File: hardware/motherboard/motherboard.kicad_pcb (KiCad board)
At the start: 4 copper layers, 152 x 68 mm, 81 parts, among them J1 IMU Connector, J2 JST-VH, J3 JST-VH, J4 JST-PH, J5 USB C 2.0, Q1 TSM7P06CP_ROG, Q2 TSM7P06CP_ROG, SW1 A, SW10 Right, SW11 Left, SW12 Up, SW2 B, SW3 X, SW4 Y, SW5 LB, SW6 RB, SW7 Start, SW8 Select, SW9 Down, U1 ESP32-S3-WROOM-1, U2 MCP73831-2-OT, U3 TPS75533KTTRG3, U4 TLV75709PDBV, U5 COM-09032

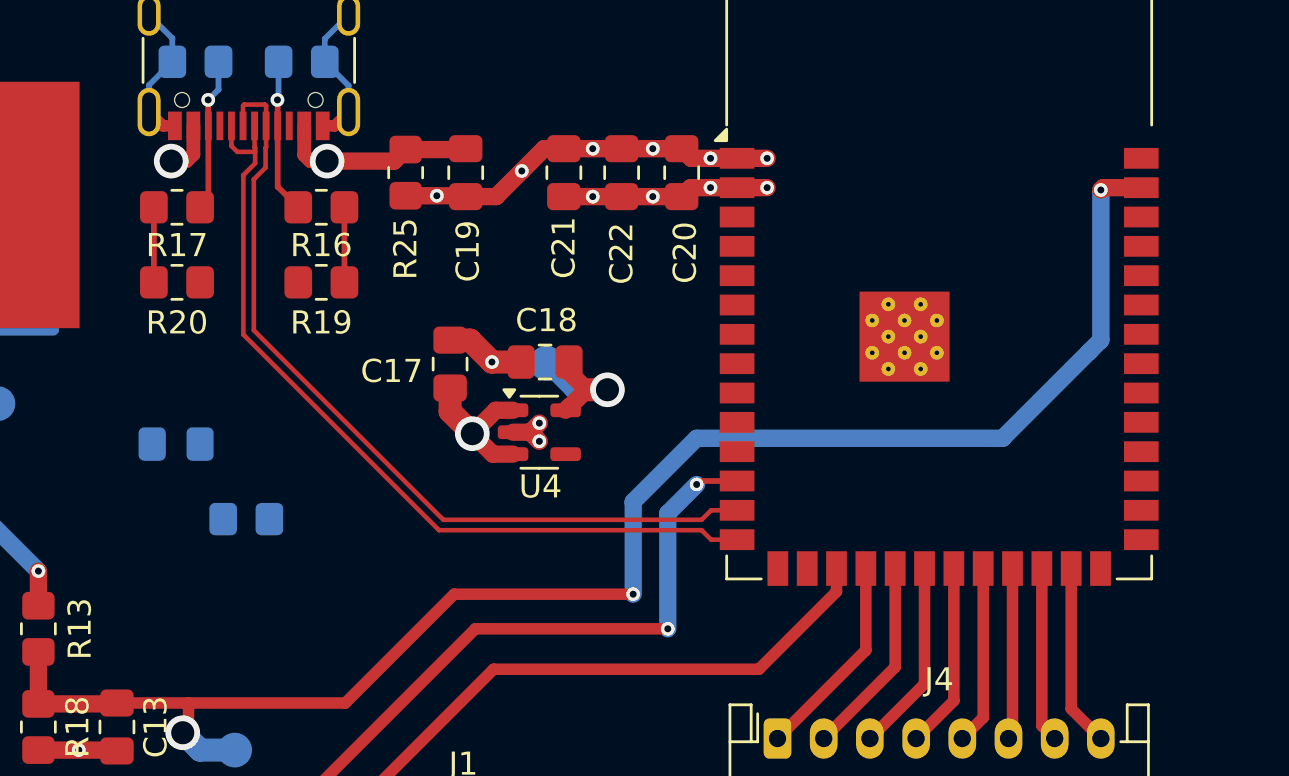
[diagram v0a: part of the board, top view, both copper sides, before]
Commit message: Reset Button
SMD Reset button on back behind MCU
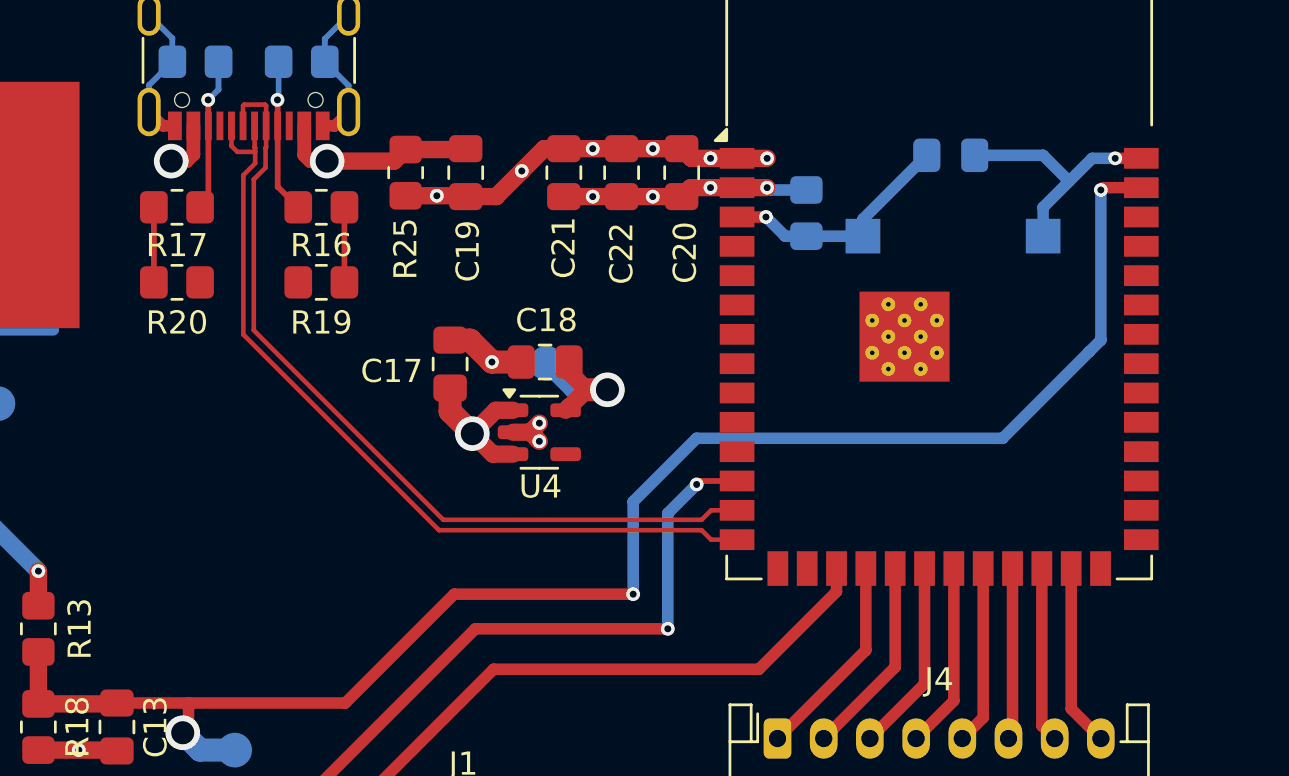
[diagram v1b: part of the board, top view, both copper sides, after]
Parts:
- added SW13: Reset, Button_Switch_SMD:SW_SPST_CK_RS282G05A3, B.Cu at (118.6, 23.2)
- moved C14 35.8 mm to (118.5, 19.8), turned to 0 degrees
- moved R14 27.6 mm to (112.2, 22.2), turned to 90 degrees
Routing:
- net GND: track 224.8 -> 235.7 mm, vias 15 -> 16
- net En: track 2.81 -> 13.5 mm, vias 0 -> 1
- net +3V3: track 34.8 -> 36.5 mm

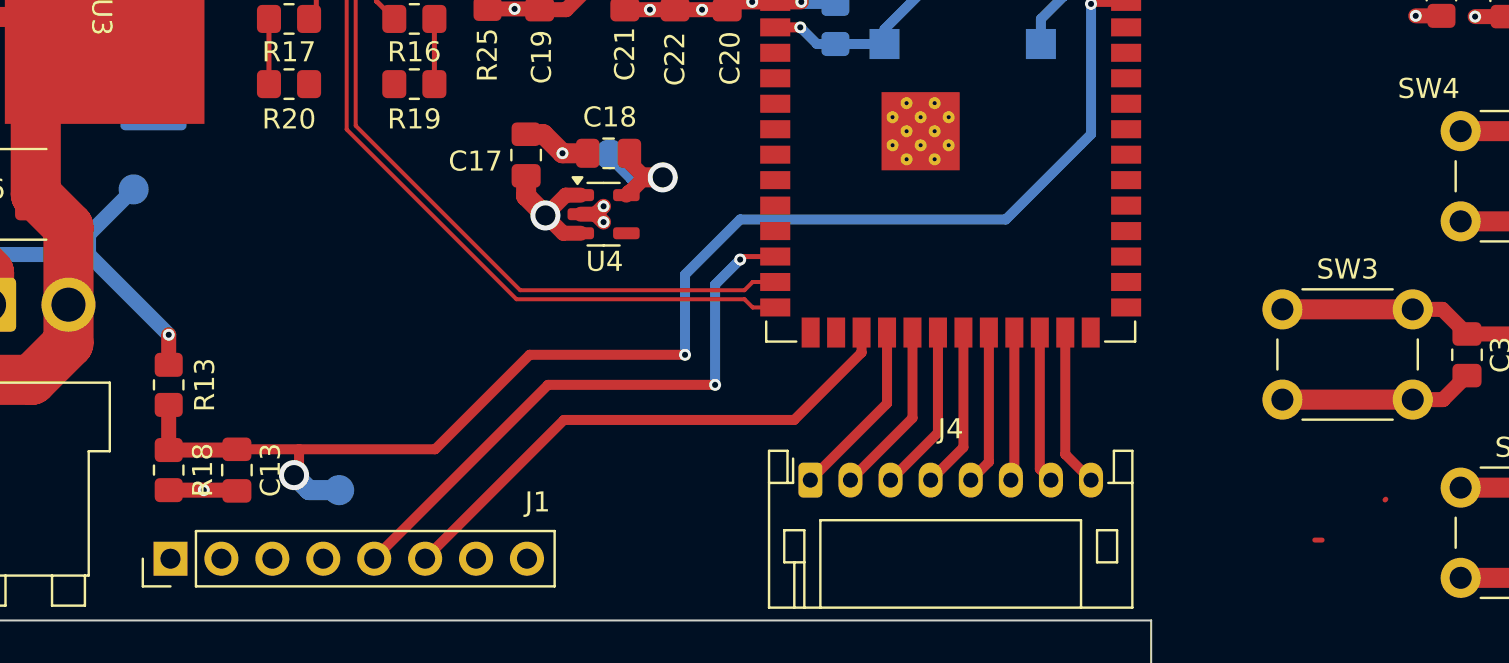
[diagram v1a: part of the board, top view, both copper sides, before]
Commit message: Added IMU Model
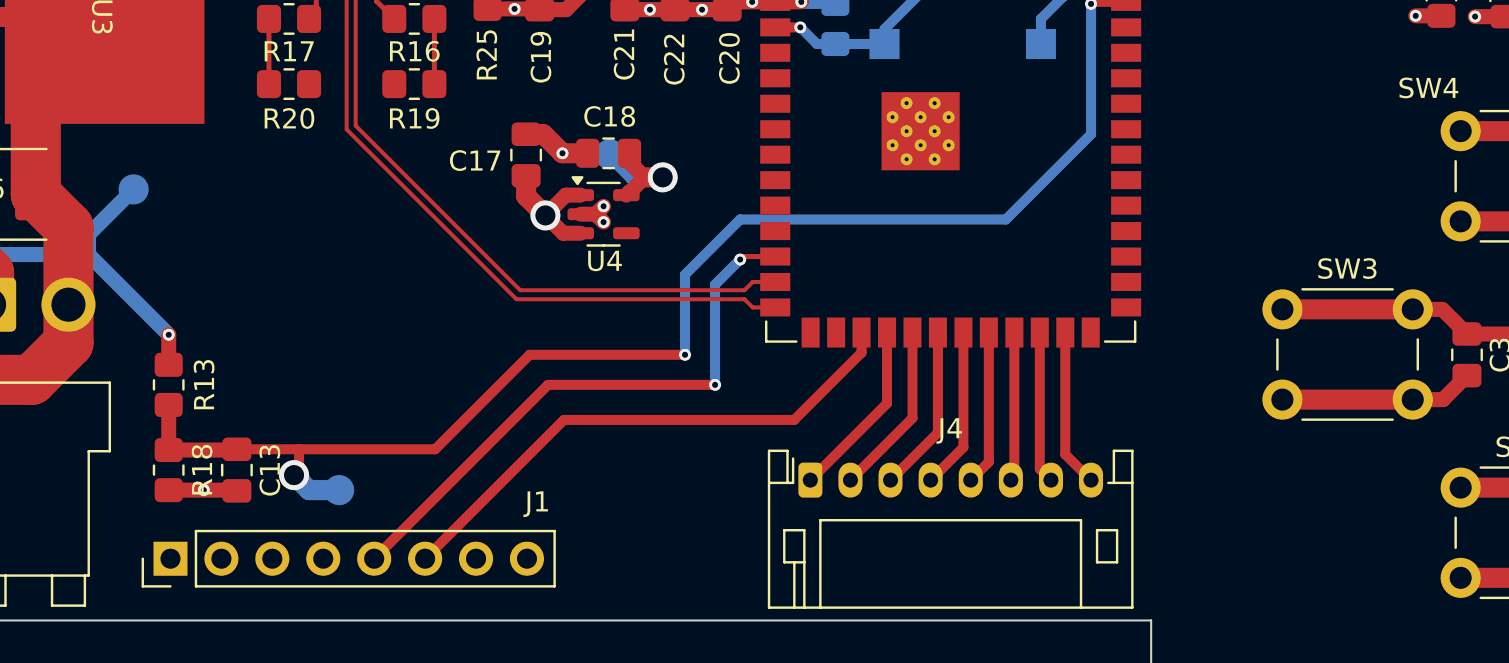
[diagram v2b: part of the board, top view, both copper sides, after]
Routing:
- net En: track 13.5 -> 10.7 mm
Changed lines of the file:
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@@
 		)
 		(embedded_fonts no)
-		(model "${KICAD9_3DMODEL_DIR}/Connector_PinHeader_2.54mm.3dshapes/PinHeader_1x08_P2.54mm_Vertical.step"
-			(hide yes)
+		(model "${OPS2_HANDHELD}/esp_32_handheld.3dshapes/MPU 6050 IMU.STEP"
 			(offset
-				(xyz 0 0 0)
+				(xyz -6.75 1.4 -8)
 			)
 			(scale
@@
 			)
 			(rotate
-				(xyz 0 0 0)
+				(xyz -90 -0 -0)
 			)
 		)
@@
 	)
 	(segment
-		(start 139.6625 45.99)
-		(end 139.7 45.9525)
-		(width 0.25)
-		(layer "F.Cu")
-		(net 1)
-	)
-	(segment
 		(start 155.9625 46.7125)
 		(end 156 46.75)
@@
 	)
 	(segment
-		(start 136.525 47.99)
-		(end 136.16 47.99)
-		(width 0.25)
-		(layer "F.Cu")
-		(net 26)
-	)
-	(segment
 		(start 109.25 21.15)
 		(end 107.2375 21.15)
@@
 		(width 0.5)
 		(layer "B.Cu")
-		(net 27)
-	)
-	(segment
-		(start 76.835 27.305)
-		(end 79.645 27.305)
-		(width 0.5)
-		(layer "B.Cu")

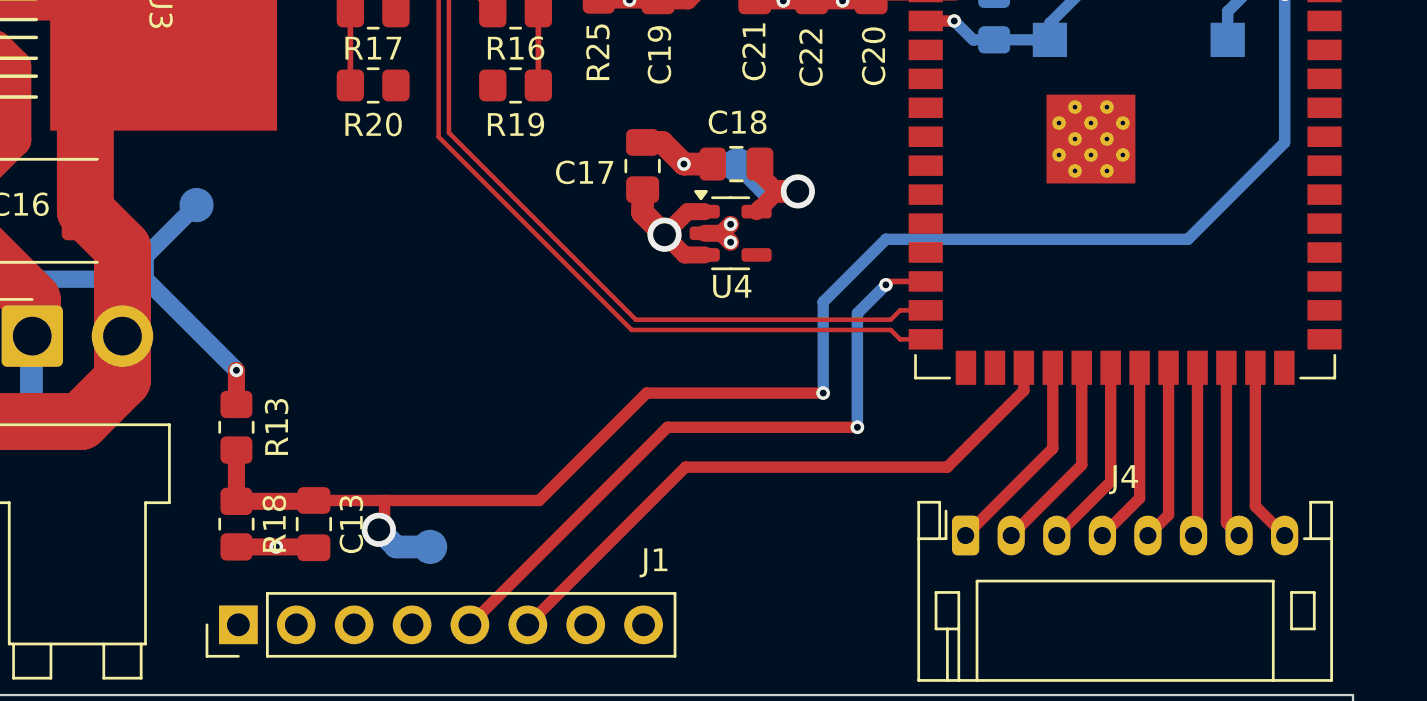
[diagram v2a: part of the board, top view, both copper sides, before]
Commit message: Moved ABat Voltage Divider
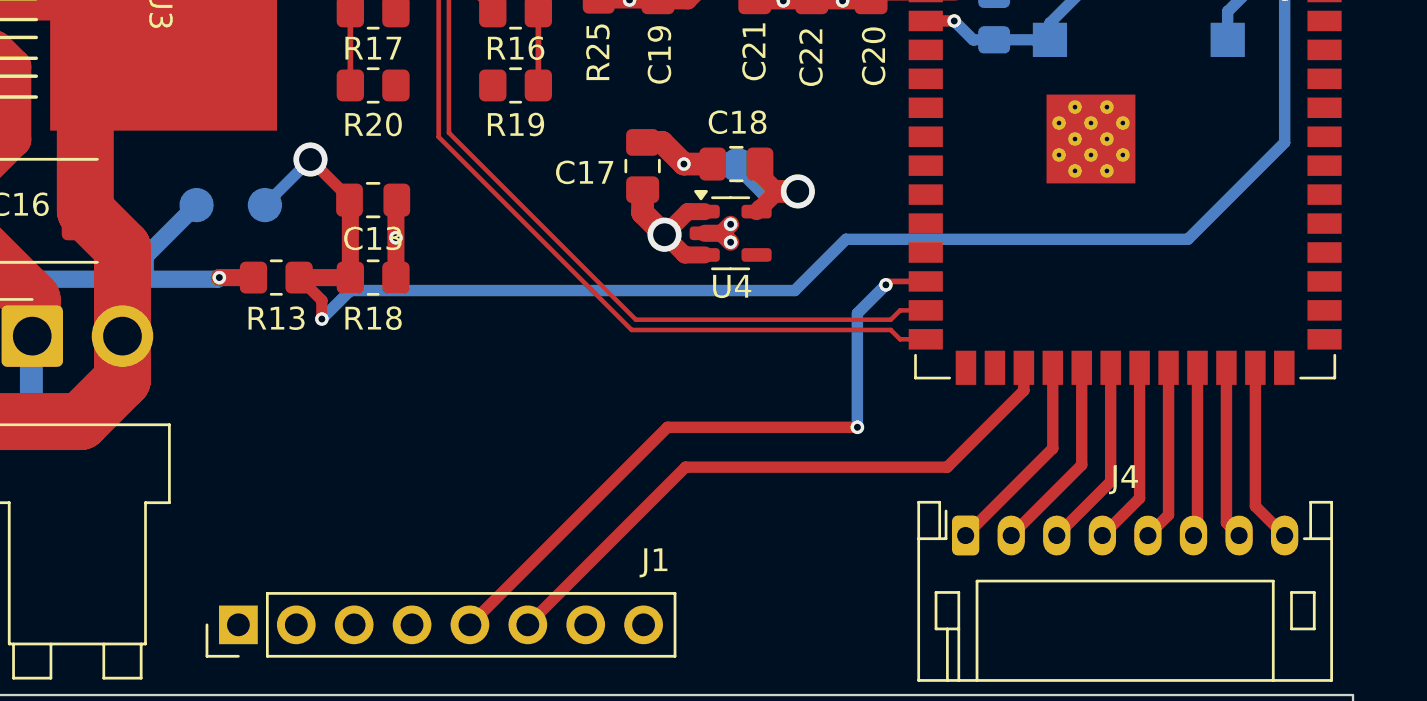
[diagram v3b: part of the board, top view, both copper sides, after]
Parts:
- moved TP1 16.7 mm to (80.2, 30.5)
- moved C13 14.5 mm to (85.0, 30.3), turned to 0 degrees
- moved R18 12.4 mm to (85.0, 33.7), turned to 0 degrees
- moved R13 6.80 mm to (80.8, 33.7), turned to 0 degrees
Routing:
- net ABat: track 69.4 -> 67.0 mm
- net VBat: track 77.7 -> 75.3 mm

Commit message: Right Side Controls Routing
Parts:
- moved J1 17.6 mm to (88.6, 58.0), turned to 180 degrees
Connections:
- U1 pad 31: unconnected-(U1-IO38-Pad31) -> BRight
- U1 pad 33: B -> X
- U1 pad 34: X -> B
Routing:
- net Start: track 13.0 -> 54.3 mm, vias 0 -> 1
- net Select/Boot: track 13.0 -> 49.0 mm
- net A: track 13.1 -> 43.1 mm
- net B: track 12.4 -> 41.7 mm
- net BRight: track 7.06 -> 28.7 mm, vias 0 -> 2
- net Y: track 13.1 -> 30.4 mm
- net X: track 13.0 -> 27.0 mm
- net SCL: track 27.0 -> 34.6 mm
- net SDA: track 29.2 -> 32.3 mm

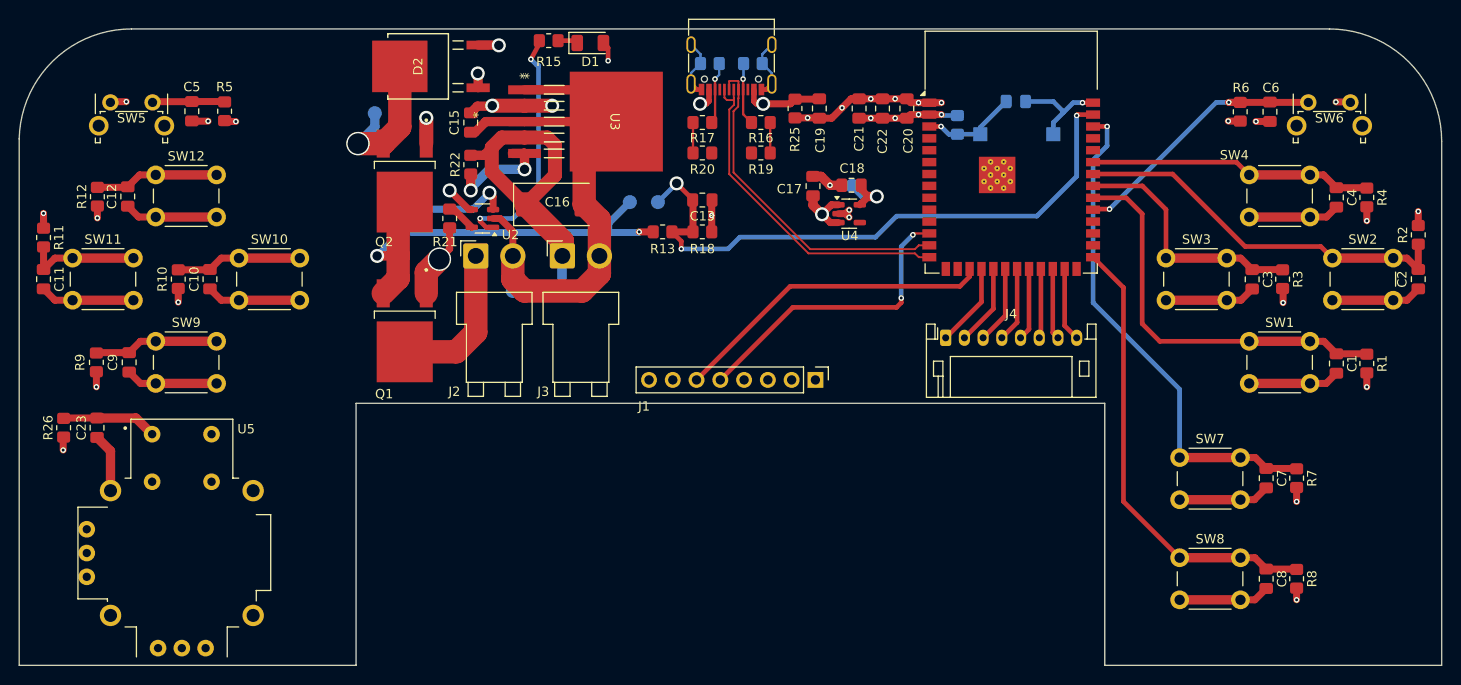
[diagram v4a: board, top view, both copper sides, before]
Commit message: Routed Joystick
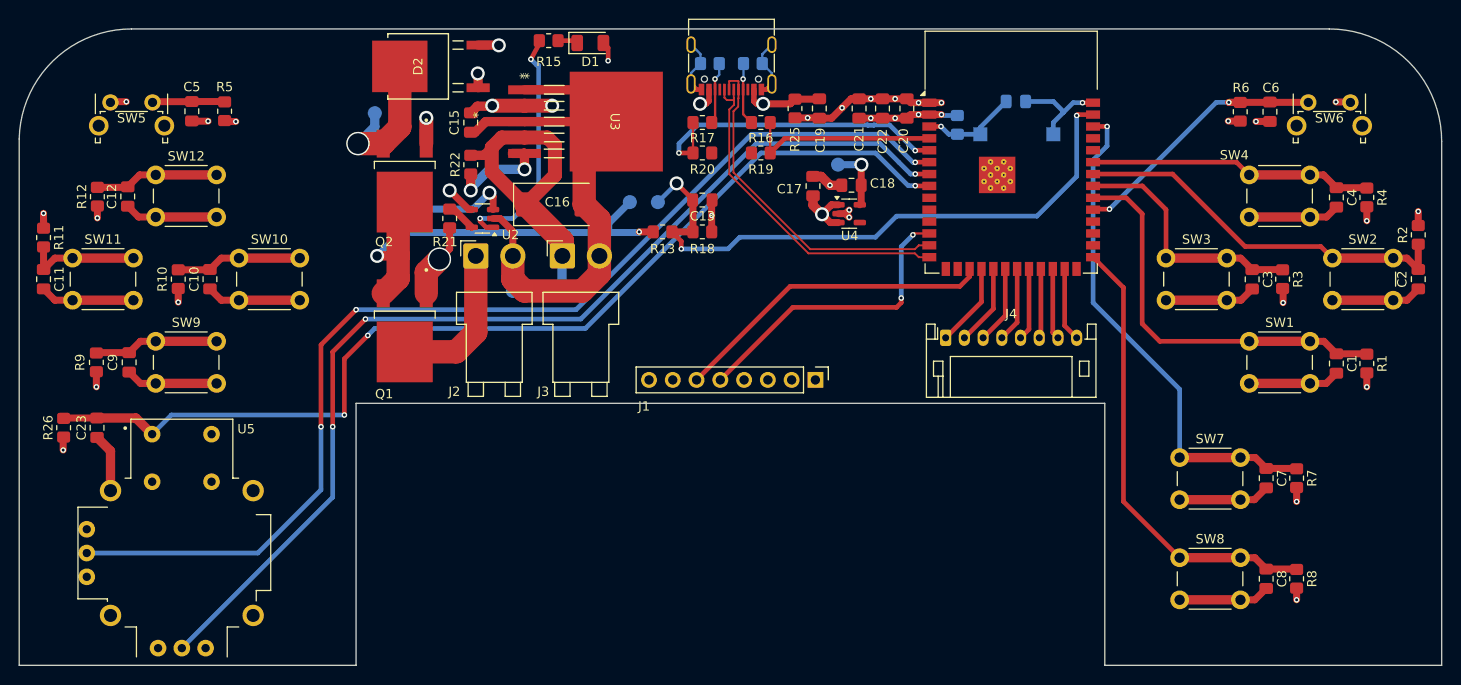
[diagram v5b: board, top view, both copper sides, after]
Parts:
- moved TP6 2.70 mm to (99.5, 26.5)
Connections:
- U1 pad 8: unconnected-(U1-IO15-Pad8) -> StckBtn
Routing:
- net AY: track 0.00 -> 118.9 mm, vias 0 -> 3
- net AX: track 0.00 -> 112.6 mm, vias 0 -> 3
- net StckBtn: track 10.2 -> 110.7 mm, vias 0 -> 3
- net ACC2: track 3.25 -> 34.5 mm, vias 0 -> 2
- net ACC1: track 3.25 -> 20.9 mm
